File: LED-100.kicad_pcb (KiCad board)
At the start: 2 copper layers, 100 x 100 mm, 100 parts, among them J2 LDA100_2_J2, J3 LDA100_2_J3, J4 LDA100_2_J4, J5 xtra, J7 Conn_01x01, J8 Conn_01x08, SW1 SW_SPDT, U1 TLC5947DAP, U2 TLC5947DAP, U3 TLC5947DAP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

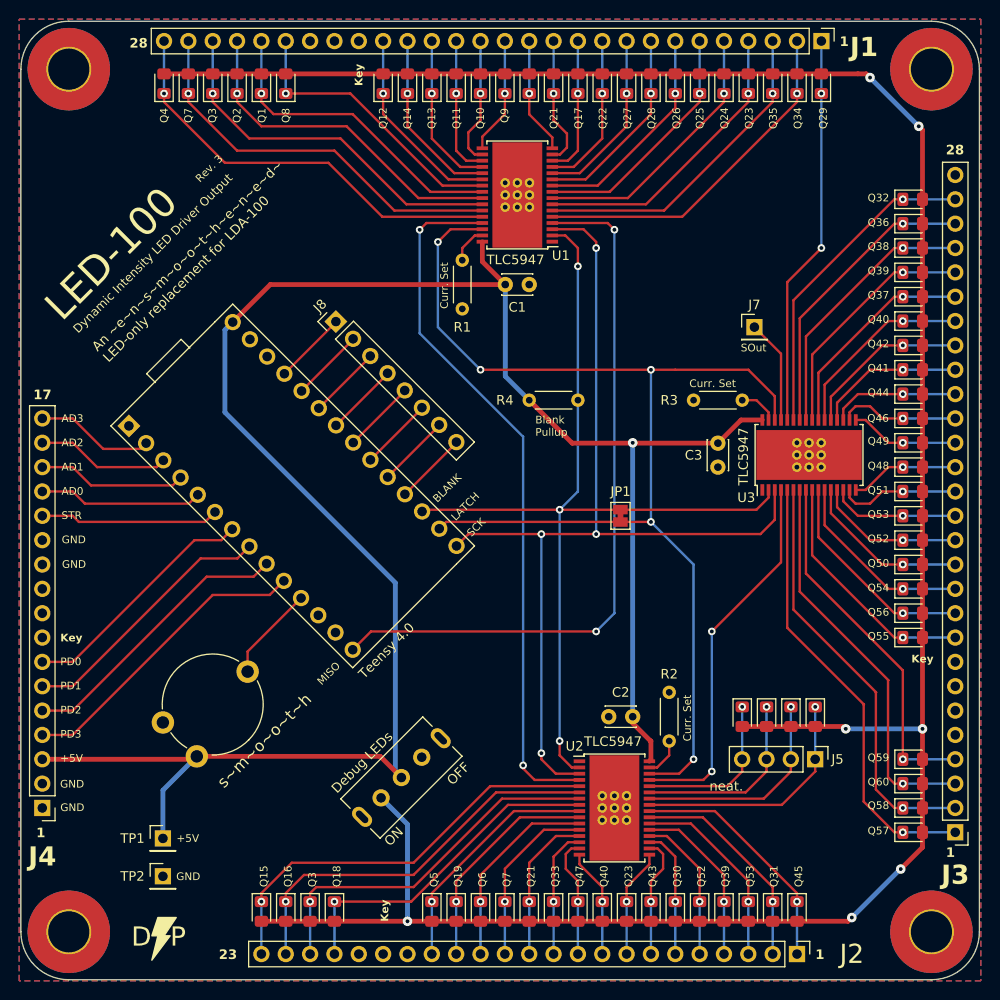
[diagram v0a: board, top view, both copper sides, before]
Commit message: added a switch, updated to kicad 9
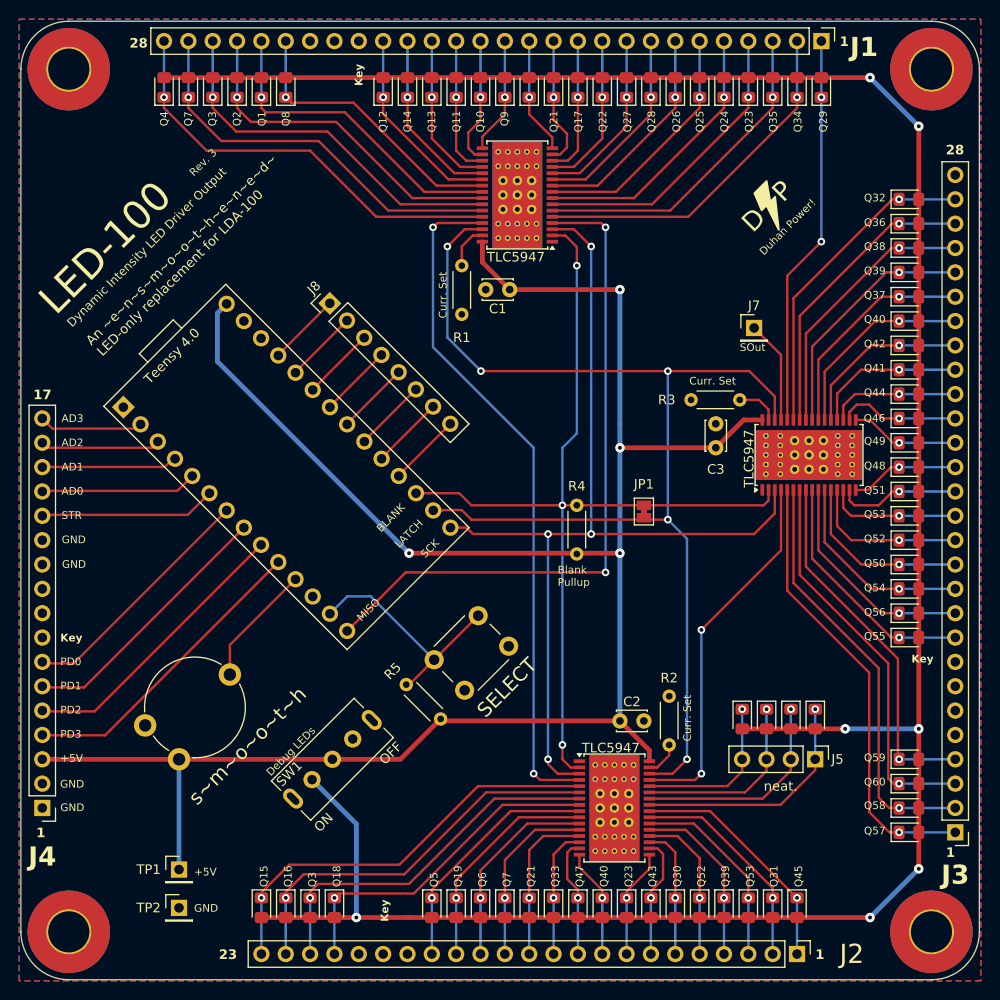
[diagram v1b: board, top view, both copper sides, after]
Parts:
- added R5: 100k, Resistor_THT:R_Axial_DIN0204_L3.6mm_D1.6mm_P5.08mm_Horizontal, F.Cu at (143.8, 122.8)
- added SELECT: SW_SPST, Button_Switch_THT:SW_PUSH_6mm_H5mm, F.Cu at (150.9, 115.2)
- SW1: footprint Button_Switch_THT:SW_Slide_SPDT_SLW-12689-4A-N-D -> MyParts:SWITCH_SPDT-SLW-12689-4A-N-D
- U1, U2, U3: footprint Package_SO:HTSSOP-32-1EP_6.1x11mm_P0.65mm_EP5.2x11mm_Mask4.11x4.36mm_ThermalVias -> MyParts:Package_SO_HTSSOP-32-1EP_6.1x11mm_P0.65mm_EP5.2x11mm_Mask4.11x4.36mm_ThermalVias
- U4: footprint Connector_PinHeader_2.54mm:PinHeader_2x1x14_P2.54mm_Vertical -> MyParts:Teensy 4.0
- moved REF** 71.0 mm to (107.5, 135.0), turned to 90 degrees
- moved R4 16.8 mm to (158.0, 105.6), turned to 90 degrees
- moved SW1 7.45 mm to (132.5, 127.0)
- moved TP2 3.70 mm to (116.5, 142.5)
- moved TP1 3.66 mm to (116.5, 138.5)
- moved JP1 2.48 mm to (165.0, 101.2)
- moved U4 2.01 mm to (126.9, 95.6)
- moved J8 2.01 mm to (132.2, 79.4)
- moved RV1 1.88 mm to (116.5, 127.0)
- moved C2 1.40 mm to (162.5, 123.0), turned to 0 degrees
- moved C1 0.71 mm to (151.0, 78.0), turned to 180 degrees
- moved R1 0.57 mm to (146.0, 75.5)
- moved C3 0.53 mm to (172.5, 94.5), turned to 90 degrees
- moved R2 0.41 mm to (167.6, 125.5)
- moved D1 0.39 mm to (125.1, 56.9)
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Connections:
- net /BLANK renamed BLANK
- net /FADESPEED renamed FADESPEED
- net /LAT renamed LAT
- net /MISO_A renamed MISO_A
- net /MISO_B renamed MISO_B
- net /MISO_C renamed MISO_C
- net /Q1 renamed Q1
- net /Q10 renamed Q10
- net /Q11 renamed Q11
- net /Q12 renamed Q12
- net /Q13 renamed Q13
- net /Q14 renamed Q14
- net /Q15 renamed Q15
- net /Q16 renamed Q16
- net /Q17 renamed Q17
- net /Q18 renamed Q18
- net /Q19 renamed Q19
- net /Q2 renamed Q2
- net /Q20 renamed Q20
- net /Q21a renamed Q21a
- net /Q21b renamed Q21b
- net /Q22 renamed Q22
- net /Q23a renamed Q23a
- net /Q23b renamed Q23b
- net /Q24 renamed Q24
- net /Q25 renamed Q25
- net /Q26 renamed Q26
- net /Q27 renamed Q27
- net /Q28 renamed Q28
- net /Q29 renamed Q29
- net /Q30 renamed Q30
- net /Q31 renamed Q31
- net /Q32 renamed Q32
- net /Q33 renamed Q33
- net /Q34 renamed Q34
- net /Q35 renamed Q35
- net /Q36 renamed Q36
- net /Q37 renamed Q37
- net /Q38 renamed Q38
- net /Q39a renamed Q39a
- net /Q39b renamed Q39b
- net /Q3a renamed Q3a
- net /Q3b renamed Q3b
- net /Q4 renamed Q4
- net /Q40a renamed Q40a
- net /Q40b renamed Q40b
- net /Q41 renamed Q41
- net /Q42 renamed Q42
- net /Q43 renamed Q43
- net /Q44 renamed Q44
- net /Q45 renamed Q45
- net /Q46 renamed Q46
- net /Q47 renamed Q47
- net /Q48 renamed Q48
- net /Q49 renamed Q49
- net /Q5 renamed Q5
- net /Q50 renamed Q50
- net /Q51 renamed Q51
- net /Q52a renamed Q52a
- net /Q52b renamed Q52b
- net /Q53a renamed Q53a
- net /Q53b renamed Q53b
- net /Q54 renamed Q54
- net /Q55 renamed Q55
- net /Q56 renamed Q56
- net /Q57 renamed Q57
- net /Q58 renamed Q58
- net /Q59 renamed Q59
- net /Q6 renamed Q6
- net /Q60 renamed Q60
- net /Q7a renamed Q7a
- net /Q7b renamed Q7b
- net /Q8 renamed Q8
- net /Q9 renamed Q9
- net /SCK renamed SCK
- net /XTRA1 renamed QX1
- net /XTRA2 renamed QX2
- net /XTRA3 renamed QX3
- net /XTRA4 renamed QX4
- U4 pad 13: unconnected-(U4-11-Pad13) -> SW_SELECT
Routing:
- net SW_SELECT: track 0.00 -> 24.8 mm
- net MISO_A: track 75.7 -> 71.1 mm
- net FADESPEED: track 9.98 -> 12.8 mm
- net MISO_B: track 73.9 -> 71.7 mm
- net Net-(J4-AD3): track 12.4 -> 10.7 mm
- net /TEST5V: track 261.9 -> 263.5 mm
- net Net-(J4-AD2): track 14.0 -> 12.5 mm
- net Net-(J4-AD1): track 15.6 -> 14.1 mm
- net Q50: track 17.6 -> 18.9 mm
- net SCK: track 101.1 -> 99.9 mm
- net Q52a: track 15.6 -> 16.7 mm
- net Q54: track 20.1 -> 21.1 mm
- net LAT: track 124.8 -> 123.8 mm
- net Q56: track 22.5 -> 23.3 mm
- net Q37: track 22.5 -> 23.3 mm
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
